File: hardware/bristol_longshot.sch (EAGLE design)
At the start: 46 parts, among them U1 SAM_D20E, U2 SI4060, U4 ADP1607ACPZN-R7, U5 S25FS-S

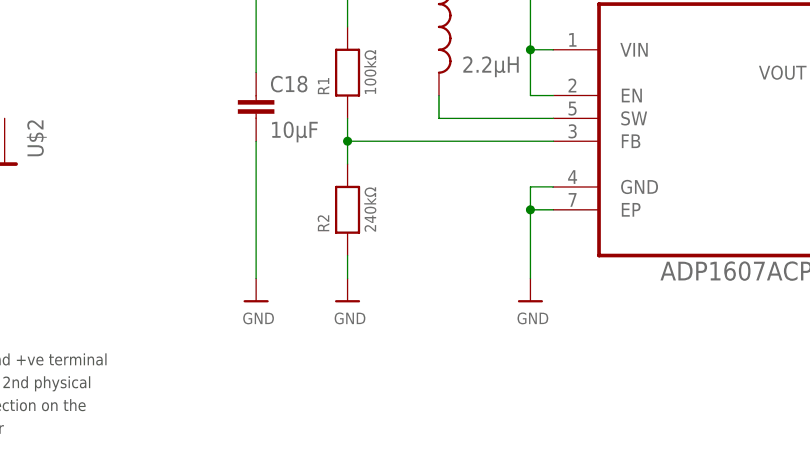
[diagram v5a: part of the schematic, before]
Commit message: Updated vcc = 2.5V for accel / gyro, updated parts list
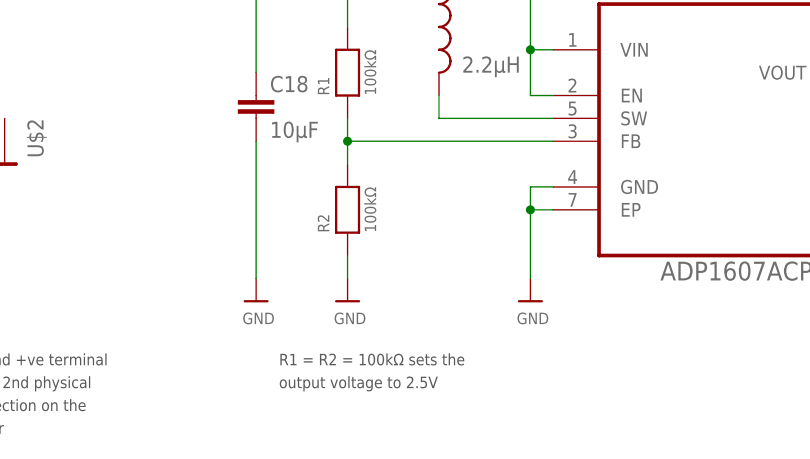
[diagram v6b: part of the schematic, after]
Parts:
- R2: value 240kΩ -> 100kΩ
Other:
- note added: "R1 = R2 = 100kΩ sets the output voltage to 2.5V"
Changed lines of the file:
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@@
 <part name="R1" library="microbuilder_v3" deviceset="RESISTOR" device="_0402" value="100kΩ"/>
 <part name="U$32" library="microbuilder_v3" deviceset="GND" device=""/>
-<part name="R2" library="microbuilder_v3" deviceset="RESISTOR" device="_0402" value="240kΩ"/>
+<part name="R2" library="microbuilder_v3" deviceset="RESISTOR" device="_0402" value="100kΩ"/>
 <part name="U$35" library="microbuilder_v3" deviceset="1.2V" device=""/>
 <part name="U$36" library="microbuilder_v3" deviceset="GND" device=""/>
@@
 <text x="93.98" y="122.174" size="1.27" layer="97" font="vector" ratio="11" rot="MR0">(SERCOM0)</text>
 <text x="93.98" y="119.634" size="1.27" layer="97" font="vector" ratio="11" rot="MR0">(TX: PAD0, TXPO: 0x0)</text>
+<text x="43.18" y="20.828" size="1.27" layer="97" font="vector" ratio="11" distance="100">R1 = R2 = 100kΩ sets the
+output voltage to 2.5V</text>
 </plain>
 <instances>
